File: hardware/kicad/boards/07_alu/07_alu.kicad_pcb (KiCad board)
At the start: 2 copper layers, 99.7 x 99.8 mm, 179 parts, among them J10 Conn_01x04_Pin, J11 Conn_01x04_Pin, J12 Conn_01x08_Pin, J15 Conn_01x08_Pin, J16 Conn_01x08_Pin, J17 Conn_01x08_Pin, J5 Conn_01x08_Pin, J6 Conn_01x08_Pin, J7 Conn_01x08_Pin, U1 74AHC541, U16 74ACT151, U2 74HC00, U3 74ACT283, U36 74HC86, U4 74HC688, U40 74LS377, U41 74ACT151, U42 74ACT151, U43 74ACT151, U44 74ACT151, U45 74ACT151, U46 74ACT151, U47 74ACT151, U48 74ACT151, U49 74ACT151, U5 74ACT283, U50 74ACT151, U51 74ACT151, U52 74ACT151, U53 74ACT151, U54 74ACT151, U55 74ACT151, U56 74ACT151, U6 74HC00

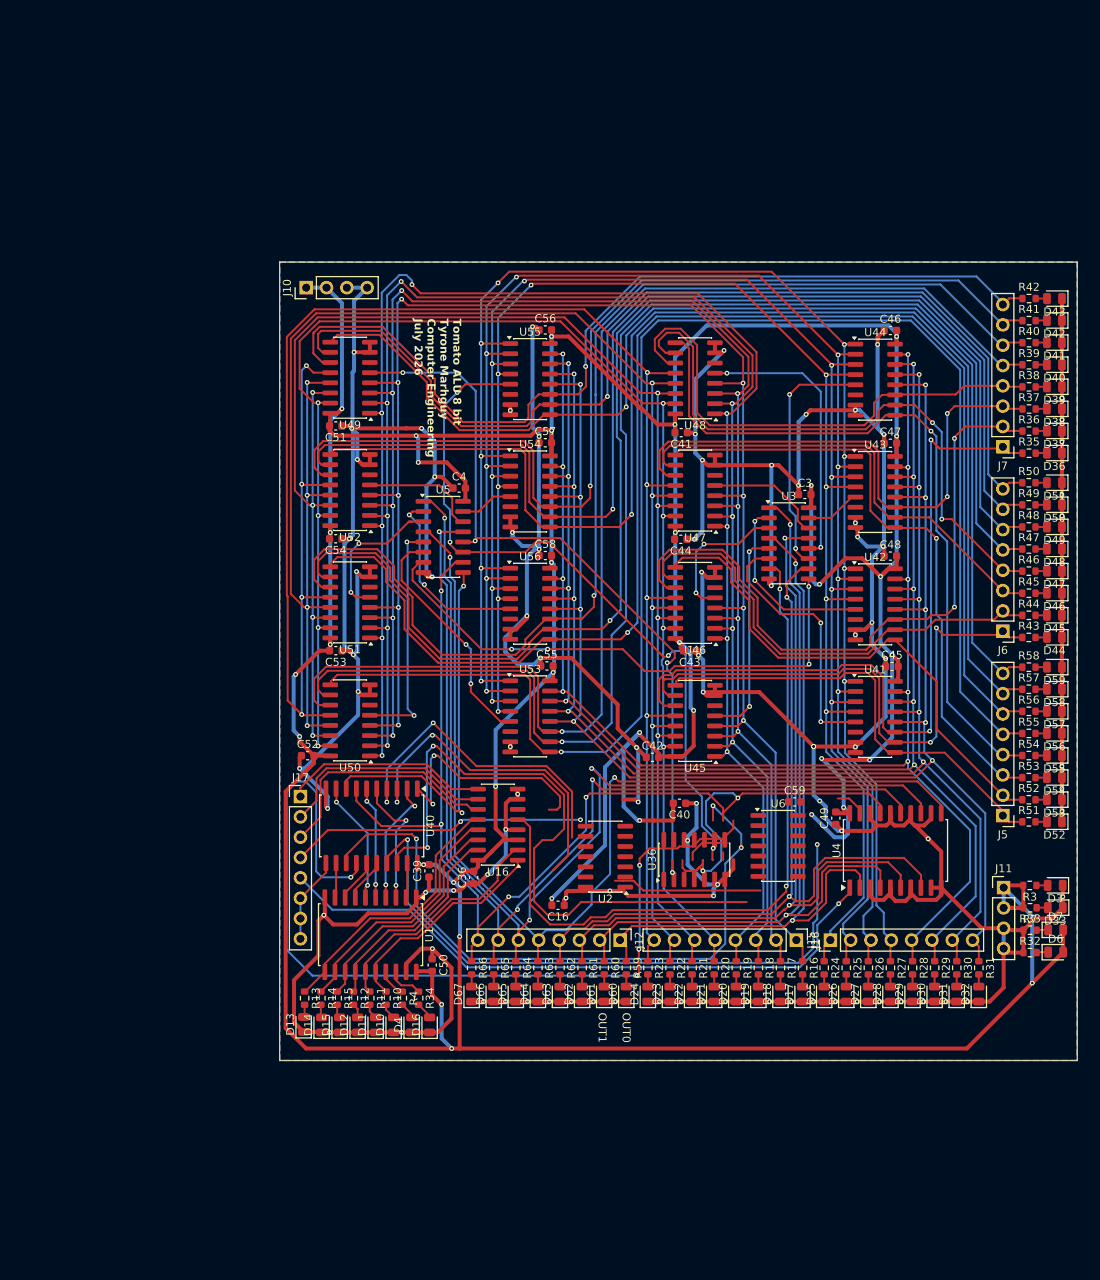
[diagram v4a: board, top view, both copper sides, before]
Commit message: feat: route 8b ALU slice and annotate pending final signoff 🎉🎉
Highlights:
- 0 ERC/DRC errors
- 0 Unrouted nets
- 2345 track segments
- 388 vias after cleanup
- 760 pads
- 18 core 74xx chips
- 7 flag 74xx chips

Pending additional confirmation of hardware-simulation faithfulness and fidelity.
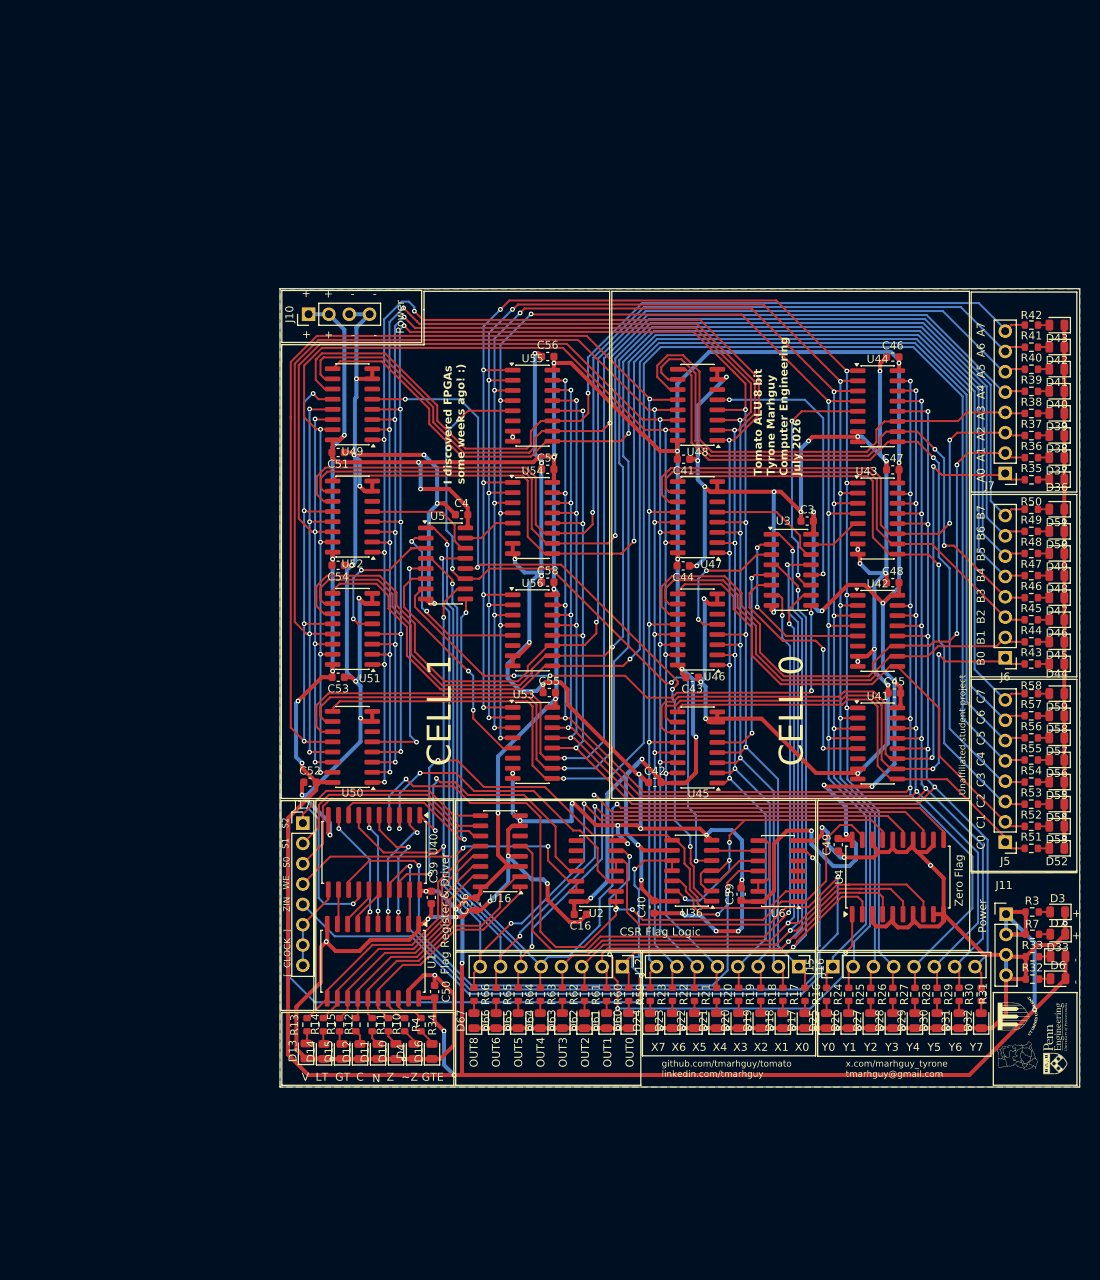
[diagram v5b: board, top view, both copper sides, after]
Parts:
- added Ref**: Val**, Graphics:ghana_map, F.Cu at (154.5, 142.6)
- added Ref**: Val**, Graphics:upenn_eng_logo, F.Cu at (159.2, 140.5)
- added Ref**: Val**, Graphics:achimota_logo, F.Cu at (154.5, 137.7)
- moved C40 13.4 mm to (109.0, 124.1), turned to 90 degrees
- moved C59 13.3 mm to (119.9, 122.5), turned to -90 degrees
- moved D23 3.33 mm to (111.3, 138.3)
- moved D25 3.33 mm to (130.6, 138.3)
- moved D26 3.33 mm to (133.4, 138.3)
- moved D29 3.33 mm to (141.7, 138.3)
- moved D30 3.33 mm to (144.4, 138.3)
- moved D31 3.33 mm to (147.2, 138.3)
- moved D61 3.33 mm to (103.1, 138.3)
- moved D66 3.33 mm to (89.3, 138.3)
- moved J12 3.33 mm to (105.1, 131.5)
- moved J16 3.33 mm to (127.1, 131.5)
- moved R17 3.33 mm to (125.2, 135.0)
- moved R23 3.33 mm to (108.6, 135.0)
- moved R26 3.33 mm to (136.1, 135.0)
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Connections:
- U2 pad 10: Net-(U2-Pad10) -> unconnected-(U2-Pad10)
- U2 pad 3: Net-(U2-Pad3) -> ZOUT
- U2 pad 4: Net-(U2-Pad3) -> ZIN
- U2 pad 6: Net-(U2-Pad10) -> ~ZIN
- U2 pad 8: ZOUT -> unconnected-(U2-Pad8)
- U2 pad 9: Net-(U2-Pad10) -> unconnected-(U2-Pad9)
- U36 pad 10: VOUT -> LT-SIGN
- U36 pad 11: GTE-SIGN -> LT-SIGN
- U36 pad 12: LT-SIGN -> VOUT
- U36 pad 13: LT-SIGN -> OUT7
- U36 pad 8: LT-SIGN -> GTE-SIGN
- U36 pad 9: OUT7 -> VCC
- U4 pad 1: ZIN -> ~ZIN
- U6 pad 10: /flags_logic/j1 -> /flags_logic/j0
- U6 pad 9: /flags_logic/j0 -> /flags_logic/j1
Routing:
- net ~ZIN: track 0.00 -> 60.5 mm, vias 0 -> 4
- net ZIN: track 79.6 -> 121.8 mm
- net ~ZOUT: track 63.2 -> 97.6 mm, vias 2 -> 4
- net GND: track 792.7 -> 824.2 mm, vias 94 -> 95
- net VCC: track 689.1 -> 710.4 mm, vias 35 -> 36
- net Net-(U6-Pad12): track 0.00 -> 8.61 mm
- net VOUT: track 83.6 -> 88.9 mm
- net GTE-SIGN: track 81.1 -> 76.1 mm
- net /flags_logic/j1: track 0.97 -> 5.78 mm
- net LT-SIGN: track 115.4 -> 111.1 mm
- net GT-SIGN: track 79.9 -> 83.4 mm
- net ~flagWE: track 29.7 -> 33.2 mm
- net FLAG_WE: track 37.0 -> 40.3 mm
- net OUT2: track 101.3 -> 98.2 mm
- net Beff: track 91.0 -> 88.0 mm
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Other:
- board size 99.7 x 99.8 mm -> 100 x 99.8 mm
- board text added: "+"
- board text added: "-"
- board text added: "A0"
- board text added: "A1"
- board text added: "A2"
- board text added: "A3"
- board text added: "A4"
- board text added: "A5"
- board text added: "A6"
- board text added: "A7"
- board text added: "B0"
- board text added: "B1"
- board text added: "B2"
- board text added: "B3"
- board text added: "B4"
- board text added: "B5"
- board text added: "B6"
- board text added: "B7"
- board text added: "C"
- board text added: "C0"
- board text added: "C1"
- board text added: "C2"
- board text added: "C3"
- board text added: "C4"
- board text added: "C5"
- board text added: "C6"
- board text added: "C7"
- board text added: "CELL 0"
- board text added: "CELL 1"
- board text added: "CSR Flag Logic"
- board text added: "Flag Register & Driver"
- board text added: "GT"
- board text added: "GTE"
- board text added: "I discovered FPGAs some weeks ago! :)"
- board text added: "LT"
- board text added: "N"
- board text added: "OUT2"
- board text added: "OUT3"
- board text added: "OUT4"
- board text added: "OUT5"
- board text added: "OUT6"
- board text added: "OUT8"
- board text added: "Power"
- board text added: "S0"
- board text added: "S1"
- board text added: "S2"
- board text added: "Unaffiliated student project"
- board text added: "V"
- board text added: "WE"
- board text added: "X0"
- board text added: "X1"
- board text added: "X2"
- board text added: "X3"
- board text added: "X4"
- board text added: "X5"
- board text added: "X6"
- board text added: "X7"
- board text added: "Y0"
- board text added: "Y1"
- board text added: "Y2"
- board text added: "Y3"
- board text added: "Y4"
- board text added: "Y5"
- board text added: "Y6"
- board text added: "Y7"
- board text added: "Z"
- board text added: "ZIN"
- board text added: "Zero Flag"
- board text added: "[ CLOCK ]"
- board text added: "github.com/tmarhguy/tomato linkedin.com/tmarhguy"
- board text added: "x.com/marhguy_tyrone tmarhguy@gmail.com"
- board text added: "~Z"
